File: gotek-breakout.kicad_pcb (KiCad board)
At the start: 2 copper layers, 101.6 x 76.5 mm, 13 parts, among them J1 FFC 10x1 0.5mm, J10 FFC 10x1 0.5mm, J11 USB Breakout, J2 USB_A, J3 OLED, J4 Encoder, J7 J7 Right Angle Connector, J8 J8 Mirror

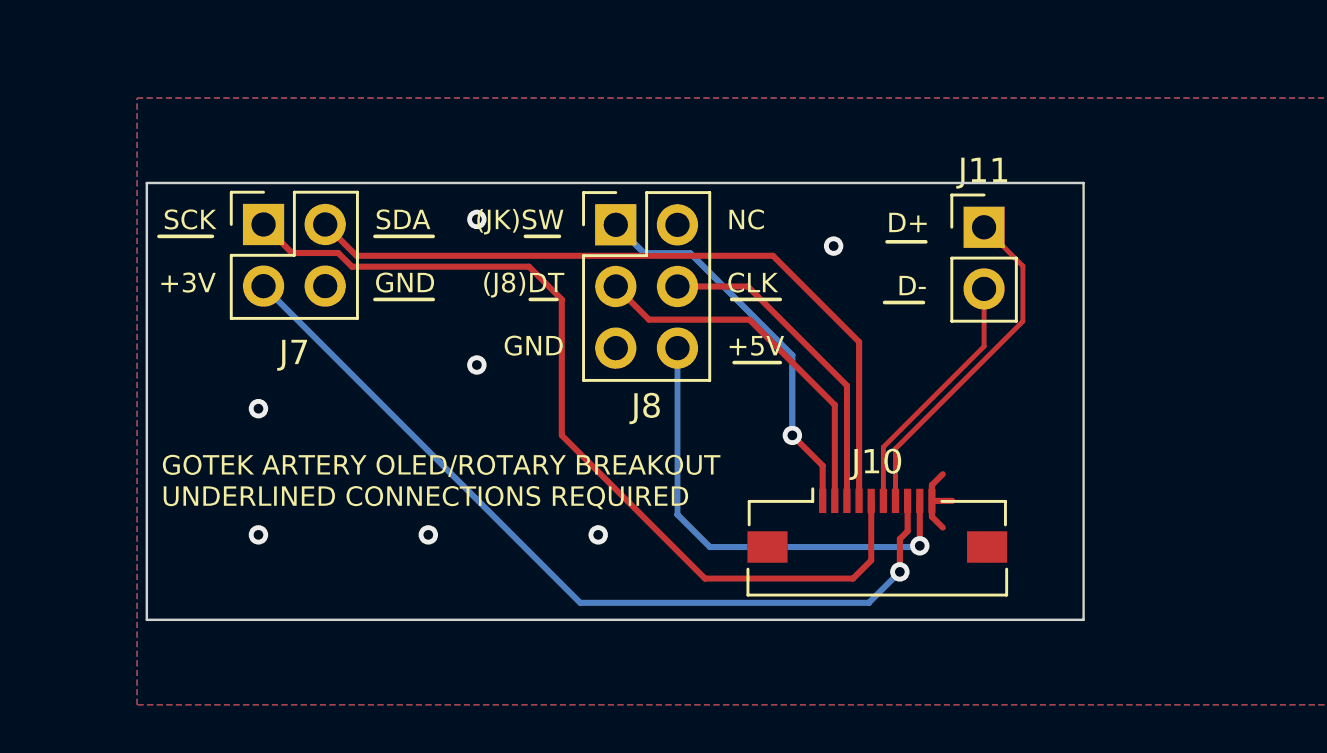
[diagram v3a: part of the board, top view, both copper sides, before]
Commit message: Add mounting to breakout, update silk
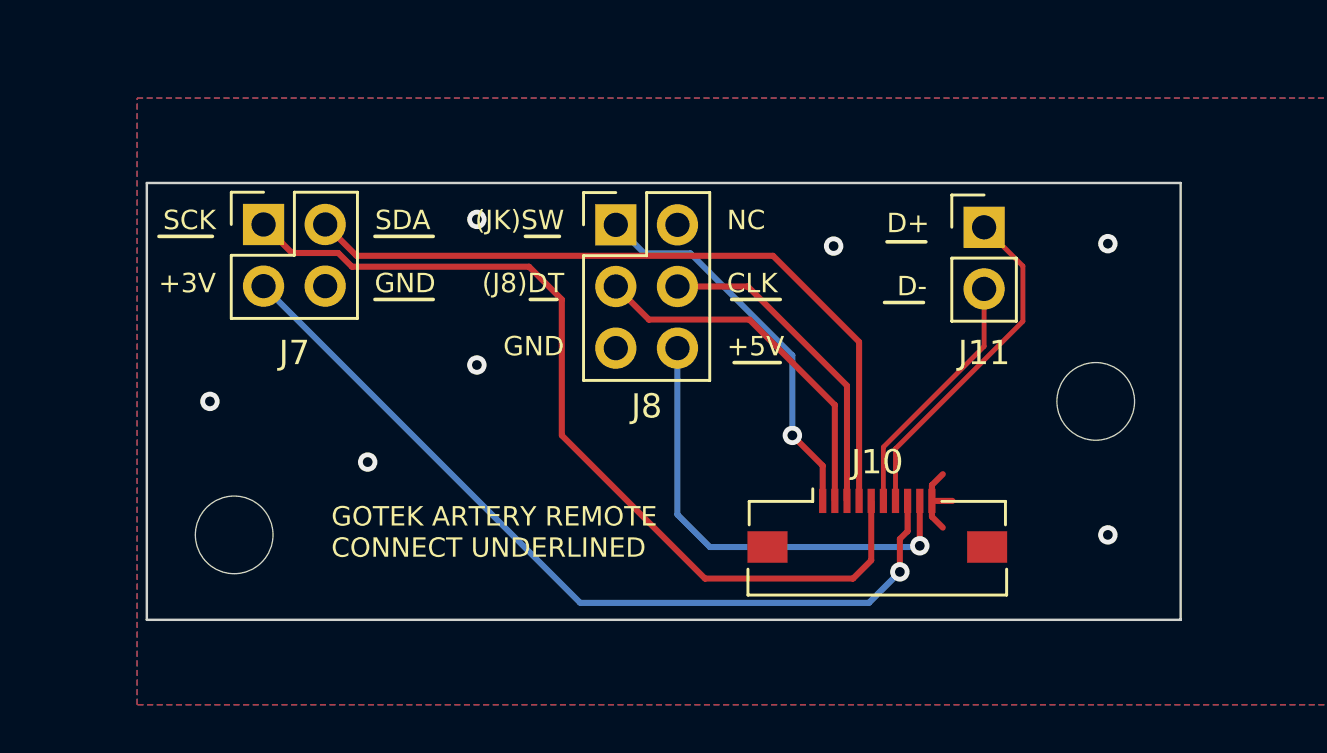
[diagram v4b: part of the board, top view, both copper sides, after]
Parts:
- added H5: MountingHole_3.2mm_M3, MountingHole:MountingHole_3.2mm_M3, F.Cu at (49.0, 113.0)
- added H6: MountingHole_3.2mm_M3, MountingHole:MountingHole_3.2mm_M3, F.Cu at (84.5, 107.5)
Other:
- outline, holes or cut-outs redrawn
- board text added: "GOTEK ARTERY REMOTE CONNECT UNDERLINED"
- board text added: "J7 CONNECTS VIA RIGHT-ANGLE 2X2 J8 JUMPER WIRE OR DUPONT J11 SOLDER TO RIGHT SIDE OF R1,R2"
- board text removed: "GOTEK ARTERY OLED/ROTARY BREAKOUT UNDERLINED CONNECTIONS REQUIRED"
- board text removed: "J7 CONNECTS VIA RIGHT-ANGLE 2X2 J8 USE DUPONT JUMPERS J11 SOLDER TO UNDERSIDE OF USB-A OR RIGHT SIDE OF R1,R2 OR PLUG USB MICRO"
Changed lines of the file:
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@@
 		)
 	)
+	(footprint "MountingHole:MountingHole_3.2mm_M3"
+		(layer "F.Cu")
+		(at 49 113)
+		(descr "Mounting Hole 3.2mm, no annular, M3")
+		(tags "mounting hole 3.2mm no annular m3")
+		(property "Reference" "H5"
+			(at 0 -4.2 0)
+			(layer "F.SilkS")
+			(hide yes)
+			(effects
+				(font
+					(size 1 1)
+					(thickness 0.15)
+				)
+			)
+		)
+		(property "Value" "MountingHole_3.2mm_M3"
+			(at 0 4.2 0)
+			(layer "F.Fab")
+			(hide yes)
+			(effects
+				(font
+					(size 1 1)
+					(thickness 0.15)
+				)
+			)
+		)
+		(property "Footprint" "MountingHole:MountingHole_3.2mm_M3"
+			(at 0 0 0)
+			(unlocked yes)
+			(layer "F.Fab")
+			(hide yes)
+			(effects
+				(font
+					(size 1.27 1.27)
+				)
+			)
+		)
+		(property "Datasheet" ""
+			(at 0 0 0)
+			(unlocked yes)
+			(layer "F.Fab")
+			(hide yes)
+			(effects
+				(font
+					(size 1.27 1.27)
+				)
+			)
+		)
+		(property "Description" ""
+			(at 0 0 0)
+			(unlocked yes)
+			(layer "F.Fab")
+			(hide yes)
+			(effects
+				(font
+					(size 1.27 1.27)
+				)
+			)
+		)
+		(attr board_only exclude_from_pos_files exclude_from_bom)
+		(fp_circle
+			(center 0 0)
+			(end 3.2 0)
+			(stroke
+				(width 0.15)
+				(type solid)
+			)
+			(fill none)
+			(layer "Cmts.User")
+		)
+		(fp_circle
+			(center 0 0)
+			(end 3.45 0)
+			(stroke
+				(width 0.05)
+				(type solid)
+			)
+			(fill none)
+			(layer "F.CrtYd")
+		)
+		(fp_text user "${REFERENCE}"
+			(at 0 0 0)
+			(layer "F.Fab")
+			(effects
+				(font
+					(size 1 1)
+					(thickness 0.15)
+				)
+			)
+		)
+		(pad "" np_thru_hole circle
+			(at 0 0)
+			(size 3.2 3.2)
+			(drill 3.2)
+			(layers "*.Cu" "*.Mask")
+		)
+	)
 	(footprint "Connector_PinHeader_2.54mm:PinHeader_2x02_P2.54mm_Vertical"
 		(layer "F.Cu")
@@
 		(tags "Through hole pin header THT 1x02 2.54mm single row")
 		(property "Reference" "J11"
-			(at 0 -2.33 0)
+			(at 0 5.175 0)
 			(layer "F.SilkS")
 			(effects
@@
 		)
 	)
+	(footprint "MountingHole:MountingHole_3.2mm_M3"
+		(layer "F.Cu")
+		(at 84.5 107.5)
+		(descr "Mounting Hole 3.2mm, no annular, M3")
+		(tags "mounting hole 3.2mm no annular m3")
+		(property "Reference" "H6"
+			(at 0 -4.2 0)
+			(layer "F.SilkS")
+			(hide yes)
+			(effects
+				(font
+					(size 1 1)
+					(thickness 0.15)
+				)
+			)
+		)
+		(property "Value" "MountingHole_3.2mm_M3"
+			(at 0 4.2 0)
+			(layer "F.Fab")
+			(hide yes)
+			(effects
+				(font
+					(size 1 1)
+					(thickness 0.15)
+				)
+			)
+		)
+		(property "Footprint" "MountingHole:MountingHole_3.2mm_M3"
+			(at 0 0 0)
+			(unlocked yes)
+			(layer "F.Fab")
+			(hide yes)
+			(effects
+				(font
+					(size 1.27 1.27)
+				)
+			)
+		)
+		(property "Datasheet" ""
+			(at 0 0 0)
+			(unlocked yes)
+			(layer "F.Fab")
+			(hide yes)
+			(effects
+				(font
+					(size 1.27 1.27)
+				)
+			)
+		)
+		(property "Description" ""
+			(at 0 0 0)
+			(unlocked yes)
+			(layer "F.Fab")
+			(hide yes)
+			(effects
+				(font
+					(size 1.27 1.27)
+				)
+			)
+		)
+		(attr board_only exclude_from_pos_files exclude_from_bom)
+		(fp_circle
+			(center 0 0)
+			(end 3.2 0)
+			(stroke
+				(width 0.15)
+				(type solid)
+			)
+			(fill none)
+			(layer "Cmts.User")
+		)
+		(fp_circle
+			(center 0 0)
+			(end 3.45 0)
+			(stroke
+				(width 0.05)
+				(type solid)
+			)
+			(fill none)
+			(layer "F.CrtYd")
+		)
+		(fp_text user "${REFERENCE}"
+			(at 0 0 0)
+			(layer "F.Fab")
+			(effects
+				(font
+					(size 1 1)
+					(thickness 0.15)
+				)
+			)
+		)
+		(pad "" np_thru_hole circle
+			(at 0 0)
+			(size 3.2 3.2)
+			(drill 3.2)
+			(layers "*.Cu" "*.Mask")
+		)
+	)
 	(footprint "Connector_FFC-FPC:Molex_54548-1071_1x10-1MP_P0.5mm_Horizontal"
 		(layer "B.Cu")
@@
 	(gr_rect
 		(start 45.4 98.5)
-		(end 84 116.5)
+		(end 88 116.5)
 		(stroke
 			(width 0.1)
@@
 		(layer "Edge.Cuts")
 	)
-	(gr_text "J7 CONNECTS VIA RIGHT-ANGLE 2X2\nJ8 USE DUPONT JUMPERS\nJ11 SOLDER TO UNDERSIDE OF USB-A\nOR RIGHT SIDE OF R1,R2\nOR PLUG USB MICRO"
-		(at 82.8 115.1 0)
+	(gr_text "J7 CONNECTS VIA RIGHT-ANGLE 2X2\nJ8 JUMPER WIRE OR DUPONT\nJ11 SOLDER TO RIGHT SIDE OF R1,R2"
+		(at 87 115 0)
 		(layer "B.SilkS")
 		(effects
@@
 	)
 	(gr_text "JLCJLCJLCJLC"
-		(at 58.3 115.5 0)
+		(at 46.630392 109.666109 -90)
 		(layer "B.SilkS")
 		(effects
@@
 		)
 	)
-	(gr_text "GOTEK ARTERY OLED/ROTARY BREAKOUT\nUNDERLINED CONNECTIONS REQUIRED"
-		(at 46 111.9 0)
+	(gr_text "GOTEK ARTERY REMOTE\nCONNECT UNDERLINED"
+		(at 53 114 0)
 		(layer "F.SilkS")
 		(effects
@@
 	)
 	(via
-		(at 57 113)
+		(at 54.5 110)
 		(size 0.8)
 		(drill 0.4)
@@
 	)
 	(via
-		(at 64 113)
+		(at 48 107.5)
 		(size 0.8)
 		(drill 0.4)
@@
 	)
 	(via
-		(at 73.7 101.1)
+		(at 85 113)
 		(size 0.8)
 		(drill 0.4)
@@
 	)
 	(via
-		(at 50 107.8)
+		(at 73.7 101.1)
 		(size 0.8)
 		(drill 0.4)
@@
 	)
 	(via
-		(at 50 113)
+		(at 85 101)
 		(size 0.8)
 		(drill 0.4)
